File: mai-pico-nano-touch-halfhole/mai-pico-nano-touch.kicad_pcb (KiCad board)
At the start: 2 copper layers, 99 x 18 mm, 5 parts, among them J1 Conn_01x04, J2 Conn_01x34, U1 MPR121-Module, U2 MPR121-Module, U3 MPR121-Module

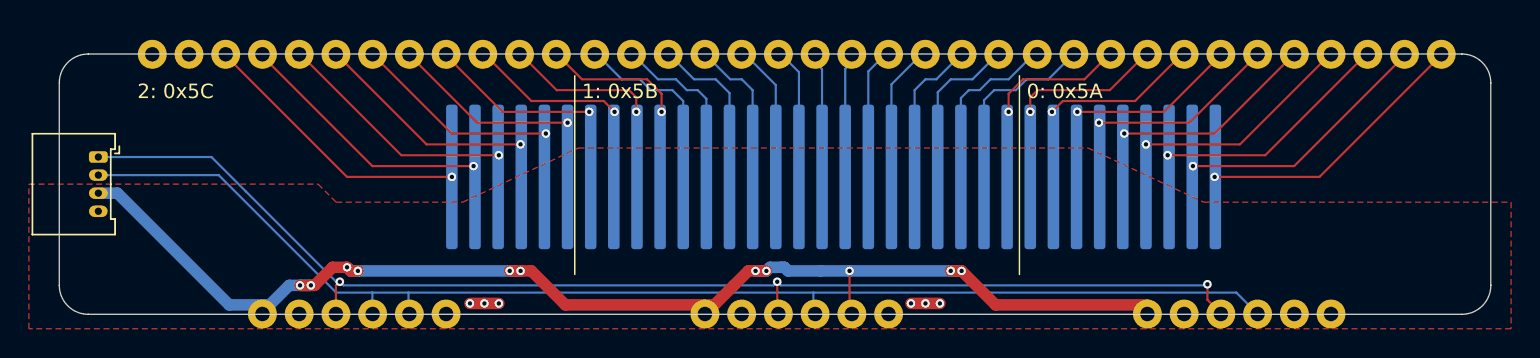
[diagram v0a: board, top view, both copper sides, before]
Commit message: Half Hole version mounting holes
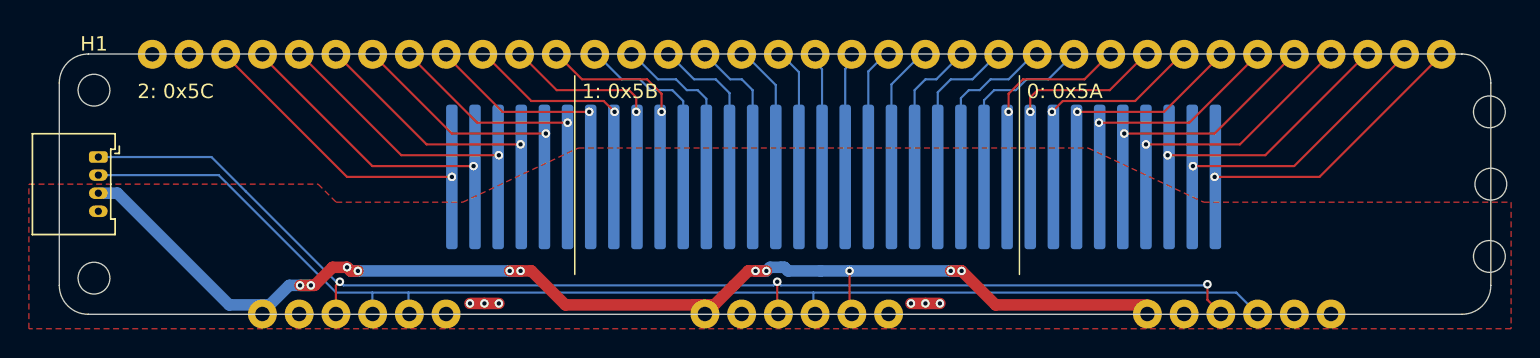
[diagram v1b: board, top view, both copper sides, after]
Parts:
- added H1: MountingHole, MountingHole:MountingHole_2.2mm_M2, F.Cu at (52.0, 76.0)
- added H2: MountingHole, MountingHole:MountingHole_2.2mm_M2, F.Cu at (52.0, 89.0)
- added H3: MountingHole, MountingHole:MountingHole_2.2mm_M2, F.Cu at (148.5, 77.5)
- added H4: MountingHole, MountingHole:MountingHole_2.2mm_M2, F.Cu at (148.5, 87.5)
- added H5: MountingHole, MountingHole:MountingHole_2.2mm_M2, F.Cu at (148.6, 82.5)
